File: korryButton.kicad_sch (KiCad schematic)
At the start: 15 parts, among them CN1 B2B-XH-A (LF)(SN), CN2 B2B-XH-A (LF)(SN), U1 SN74AHCT125DR, U2 B3B-XH-A(LF)(SN), U3 WS2811C, U4 WS2811C

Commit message: update
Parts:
- removed KEY1: ，12×12x7.3，:2.55N，:0.3mm, lcsc_footprints:C84931_KEY-TH_4P-L12_0-W12_0-P5_00-LS13_4-EH, symbol lcsc_imported:，12×12x7_3，{colon}2_55N，{colon}0_3mm
- added SW1: 5.8 ZSGT, lcsc_footprints:C2681587_SW-TH_5_8ZSGT, symbol lcsc_imported:5_8_ZSGT
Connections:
- net VCC: now also SW1.1
- net at R2.2: now also SW1.2
- net at C1.1, R1.1: now also SW1.3
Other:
- moved on the sheet: C1, R1, R2, R3

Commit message: update schematic, pcb
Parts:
- removed CN1, CN2: B2B-XH-A (LF)(SN), lcsc_footprints:C158012_CONN-TH_B2B-XH-A-LF-SN, symbol lcsc_imported:B2B-XH-A_(LF)(SN)
- removed U2: B3B-XH-A(LF)(SN), lcsc_footprints:C144394_CONN-TH_3P-P2_50_A2501WV2-3P, symbol lcsc_imported:B3B-XH-A(LF)(SN)
- added C4: 100nF (104) ±10% 50V, lcsc_footprints:C1591_C0603, symbol lcsc_imported:100nF_(104)_±10%_50V
- added CN1: B5B-XH-A (LF)(SN), lcsc_footprints:C157991_CONN-TH_B5B-XH-A-LF-SN, symbol lcsc_imported:B5B-XH-A_(LF)(SN)
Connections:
- net GND: now also C4.1, CN1.2
- net VCC: now also C4.2, CN1.1
- net at U1.2 (1A): now also CN1.4
- net at R2.1, R3.2: now also CN1.5
- net at U4.5 (DO): now also CN1.3
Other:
- note removed: "DIN"

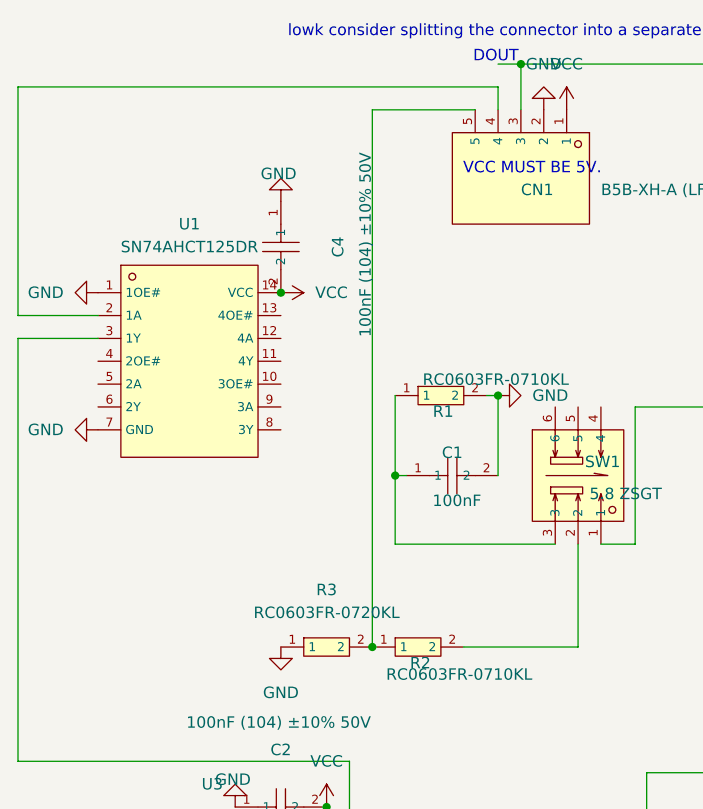
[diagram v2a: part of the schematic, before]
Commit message: update C1 position, pcb layout
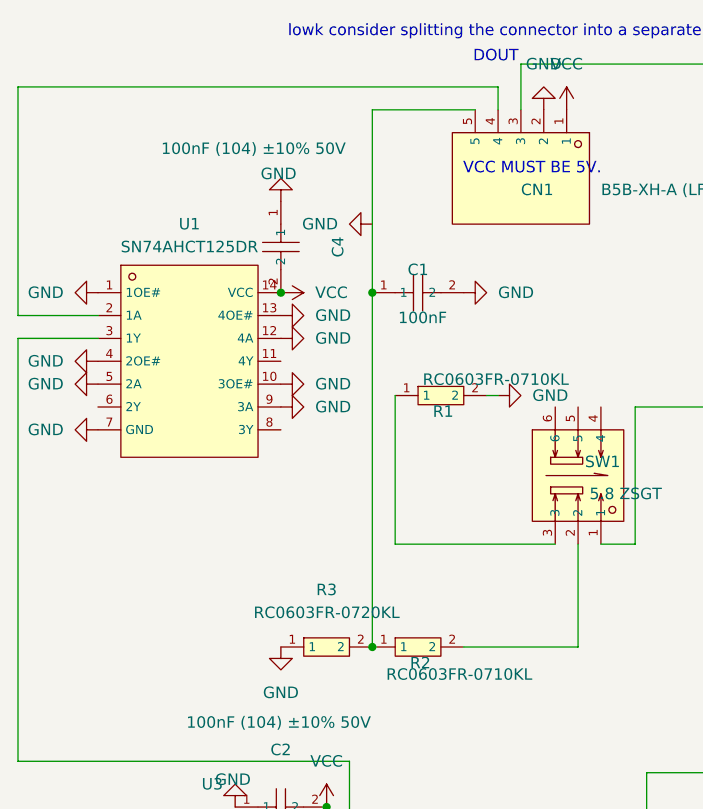
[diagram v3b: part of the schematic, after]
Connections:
- net GND: now also U1.10 (3OE#), U1.12 (4A), U1.13 (4OE#), U1.4 (2OE#), U1.5 (2A), U1.9 (3A)
- net at CN1.5, R2.1, R3.2: now also C1.1
- net at R1.1, SW1.3: no longer C1.1

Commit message: update resistor schematics to fix erc errors
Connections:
- no-connect marks 0 -> 8
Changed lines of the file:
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@@
+	)
+	(junction
+		(at 78.74 49.53)
+		(diameter 0)
+		(color 0 0 0 0)
 	)
 	(junction
@@
 		(diameter 0)
 		(color 0 0 0 0)
+	)
+	(junction
+		(at 76.2 49.53)
+		(diameter 0)
+		(color 0 0 0 0)
+	)
+	(no_connect
+		(at 26.67 82.55)
+	)
+	(no_connect
+		(at 77.47 82.55)
+	)
+	(no_connect
+		(at 46.99 77.47)
+	)
+	(no_connect
+		(at 52.07 134.62)
+	)
+	(no_connect
+		(at 82.55 82.55)
+	)
+	(no_connect
+		(at 46.99 85.09)
+	)
+	(no_connect
+		(at 80.01 82.55)
+	)
+	(no_connect
+		(at 129.54 134.62)
 	)
 	(wire
@@
 	)
 	(symbol
+		(lib_id "power:PWR_FLAG")
+		(at 78.74 49.53 270)
+		(unit 1)
+		(body_style 1)
+		(exclude_from_sim no)
+		(in_bom yes)
+		(on_board yes)
+		(in_pos_files yes)
+		(dnp no)
+		(fields_autoplaced yes)
+		(property "Reference" "#FLG01"
+			(at 80.645 49.53 0)
+			(hide yes)
+			(show_name no)
+			(do_not_autoplace no)
+			(effects
+				(font
+					(size 1.27 1.27)
+				)
+			)
+		)
+		(property "Value" "PWR_FLAG"
+			(at 82.55 49.5299 90)
+			(show_name no)
+			(do_not_autoplace no)
+			(effects
+				(font
+					(size 1.27 1.27)
+				)
+				(justify left)
+			)
+		)
+		(property "Footprint" ""
+			(at 78.74 49.53 0)
+			(hide yes)
+			(show_name no)
+			(do_not_autoplace no)
+			(effects
+				(font
+					(size 1.27 1.27)
+				)
+			)
+		)
+		(property "Datasheet" ""
+			(at 78.74 49.53 0)
+			(hide yes)
+			(show_name no)
+			(do_not_autoplace no)
+			(effects
+				(font
+					(size 1.27 1.27)
+				)
+			)
+		)
+		(property "Description" "Special symbol for telling ERC where power comes from"
+			(at 78.74 49.53 0)
+			(hide yes)
+			(show_name no)
+			(do_not_autoplace no)
+			(effects
+				(font
+					(size 1.27 1.27)
+				)
+			)
+		)
+		(pin "1"
+		)
+		(instances
+			(project "korryButton"
+				(path "/bfc9e741-6c13-4327-93fc-8e179bada6f9"
+					(reference "#FLG01")
+					(unit 1)
+				)
+			)
+		)
+	)
+	(symbol
 		(lib_id "lcsc_imported:XL-B504RGBW")
 		(at 116.84 153.67 0)
@@
 				(path "/bfc9e741-6c13-4327-93fc-8e179bada6f9"
 					(reference "LED2")
-					(unit 1)
-				)
-			)
-		)
-	)
-	(symbol
-		(lib_id "power:GND")
-		(at 57.15 62.23 270)
-		(unit 1)
-		(body_style 1)
-		(exclude_from_sim no)
-		(in_bom yes)
-		(on_board yes)
-		(in_pos_files yes)
-		(dnp no)
-		(fields_autoplaced yes)
-		(property "Reference" "#PWR026"
-			(at 50.8 62.23 0)
-			(hide yes)
-			(show_name no)
-			(do_not_autoplace no)
-			(effects
-				(font
-					(size 1.27 1.27)
-				)
-			)
-		)
-		(property "Value" "GND"
-			(at 53.34 62.2299 90)
-			(show_name no)
-			(do_not_autoplace no)
-			(effects
-				(font
-					(size 1.27 1.27)
-				)
-				(justify right)
-			)
-		)
-		(property "Footprint" ""
-			(at 57.15 62.23 0)
-			(hide yes)
-			(show_name no)
-			(do_not_autoplace no)
-			(effects
-				(font
-					(size 1.27 1.27)
-				)
-			)
-		)
-		(property "Datasheet" ""
-			(at 57.15 62.23 0)
-			(hide yes)
-			(show_name no)
-			(do_not_autoplace no)
-			(effects
-				(font
-					(size 1.27 1.27)
-				)
-			)
-		)
-		(property "Description" "Power symbol creates a global label with name \"GND\" , ground"
-			(at 57.15 62.23 0)
-			(hide yes)
-			(show_name no)
-			(do_not_autoplace no)
-			(effects
-				(font
-					(size 1.27 1.27)
-				)
-			)
-		)
-		(pin "1"
-		)
-		(instances
-			(project "korryButton"
-				(path "/bfc9e741-6c13-4327-93fc-8e179bada6f9"
-					(reference "#PWR026")
 					(unit 1)
 				)
@@
 					(unit 1)
 				)
+			)
+		)
+	)
+	(symbol
+		(lib_id "power:PWR_FLAG")
+		(at 76.2 49.53 90)
+		(unit 1)
+		(body_style 1)
+		(exclude_from_sim no)
+		(in_bom yes)
+		(on_board yes)
+		(in_pos_files yes)
+		(dnp no)
+		(fields_autoplaced yes)
+		(property "Reference" "#FLG02"
+			(at 74.295 49.53 0)
+			(hide yes)
+			(show_name no)
+			(do_not_autoplace no)
+			(effects
+				(font
+					(size 1.27 1.27)
+				)
+			)
+		)
+		(property "Value" "PWR_FLAG"
+			(at 72.39 49.5299 90)
+			(show_name no)
+			(do_not_autoplace no)
+			(effects
+				(font
+					(size 1.27 1.27)
+				)
+				(justify left)
+			)
+		)
+		(property "Footprint" ""
+			(at 76.2 49.53 0)
+			(hide yes)
+			(show_name no)
+			(do_not_autoplace no)
+			(effects
+				(font
+					(size 1.27 1.27)
+				)
+			)
+		)
+		(property "Datasheet" ""
+			(at 76.2 49.53 0)
+			(hide yes)
+			(show_name no)
+			(do_not_autoplace no)
+			(effects
+				(font
+					(size 1.27 1.27)
+				)
+			)
+		)
+		(property "Description" "Special symbol for telling ERC where power comes from"
+			(at 76.2 49.53 0)
+			(hide yes)
+			(show_name no)
+			(do_not_autoplace no)
+			(effects
+				(font
+					(size 1.27 1.27)
+				)
+			)
+		)
+		(pin "1"
+		)
+		(instances
+			(project "korryButton"
+				(path "/bfc9e741-6c13-4327-93fc-8e179bada6f9"
+					(reference "#FLG02")
+					(unit 1)
+				)

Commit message: udpate leds to be DNP
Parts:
- LED1, LED2: now not fitted; now left out of the parts list
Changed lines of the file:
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@@
 		(body_style 1)
 		(exclude_from_sim no)
-		(in_bom yes)
-		(on_board yes)
-		(in_pos_files yes)
-		(dnp no)
+		(in_bom no)
+		(on_board yes)
+		(in_pos_files no)
+		(dnp yes)
 		(fields_autoplaced yes)
 		(property "Reference" "LED2"
@@
 		(body_style 1)
 		(exclude_from_sim no)
-		(in_bom yes)
-		(on_board yes)
-		(in_pos_files yes)
-		(dnp no)
+		(in_bom no)
+		(on_board yes)
+		(in_pos_files no)
+		(dnp yes)
 		(fields_autoplaced yes)
 		(property "Reference" "LED1"

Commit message: update pcb for prod, prod finished
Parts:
- CN1: now not fitted; now left out of the parts list
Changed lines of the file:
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@@
 		(body_style 1)
 		(exclude_from_sim no)
-		(in_bom yes)
+		(in_bom no)
 		(on_board yes)
-		(in_pos_files yes)
-		(dnp no)
+		(in_pos_files no)
+		(dnp yes)
 		(property "Reference" "CN1"
 			(at 73.66 58.42 90)
